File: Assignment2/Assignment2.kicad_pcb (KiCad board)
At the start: 2 copper layers, 1 part, among them U1 RP2040

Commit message: assignment2: microphone and color module
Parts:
- added C1: 10μF, Capacitor_SMD:C_0603_1608Metric, F.Cu at (106.5, 68.9)
- added C10: 100nF, Capacitor_SMD:C_0603_1608Metric, F.Cu at (106.5, 81.4)
- added C11: 100nF, Capacitor_SMD:C_0603_1608Metric, F.Cu at (106.5, 83.9)
- added C12: 100nF, Capacitor_SMD:C_0603_1608Metric, F.Cu at (110.5, 68.9)
- added C13: 100nF, Capacitor_SMD:C_0603_1608Metric, F.Cu at (110.5, 71.4)
- added C14: 100nF, Capacitor_SMD:C_0603_1608Metric, F.Cu at (110.5, 73.9)
- added C15: 100nF, Capacitor_SMD:C_0603_1608Metric, F.Cu at (110.5, 76.4)
- added C16: 100nF, Capacitor_SMD:C_0603_1608Metric, F.Cu at (110.5, 78.9)
- added C17: 10μF, Capacitor_SMD:C_0603_1608Metric, F.Cu at (110.5, 81.4)
- added C18: 0.1μF, Capacitor_SMD:C_0603_1608Metric, F.Cu at (110.5, 83.9)
- added C19: 0.1μF, Capacitor_SMD:C_0603_1608Metric, F.Cu at (114.6, 68.9)
- added C2: 10μF, Capacitor_SMD:C_0603_1608Metric, F.Cu at (106.5, 71.4)
- added C20: 200pF, Capacitor_SMD:C_0603_1608Metric, F.Cu at (114.6, 71.4)
- added C21: 100nF, Capacitor_SMD:C_0603_1608Metric, F.Cu at (114.6, 73.9)
- added C3: 100μF, Capacitor_SMD:C_0603_1608Metric, F.Cu at (106.5, 73.9)
- added C4: 15pF, Capacitor_SMD:C_0402_1005Metric, F.Cu at (120.9, 91.2)
- added C5: 15pF, Capacitor_SMD:C_0402_1005Metric, F.Cu at (120.9, 93.2)
- added C6: 1μF, Capacitor_SMD:C_0402_1005Metric, F.Cu at (120.9, 95.2)
- added C7: 100nF, Capacitor_SMD:C_0603_1608Metric, F.Cu at (106.5, 76.4)
- added C8: 100nF, Capacitor_SMD:C_0603_1608Metric, F.Cu at (106.5, 78.9)
- added C9: 1μF, Capacitor_SMD:C_0402_1005Metric, F.Cu at (120.9, 97.1)
- added H1: MountingHole, MountingHole:MountingHole_2.7mm_M2.5, F.Cu at (101.1, 71.1)
- added H2: MountingHole, MountingHole:MountingHole_2.7mm_M2.5, F.Cu at (101.1, 78.0)
- added H3: MountingHole, MountingHole:MountingHole_2.7mm_M2.5, F.Cu at (101.1, 85.0)
- added H4: MountingHole, MountingHole:MountingHole_2.7mm_M2.5, F.Cu at (101.1, 91.9)
- added J1: USB_B_Micro, Connector_USB:USB_Micro-B_Amphenol_10103594-0001LF_Horizontal, F.Cu at (125.3, 79.8)
- added J2: Conn_01x02, Connector_PinSocket_2.54mm:PinSocket_1x02_P2.54mm_Vertical, F.Cu at (106.9, 94.4)
- added J3: Conn_01x03, Connector_PinSocket_2.54mm:PinSocket_1x03_P2.54mm_Vertical, F.Cu at (117.2, 92.6)
- added J4: Conn_01x02, Connector_PinSocket_2.54mm:PinSocket_1x02_P2.54mm_Vertical, F.Cu at (111.5, 94.4)
- added MK1: SPH0645LM4H, Sensor_Audio:Knowles_SPH0645LM4H-6_3.5x2.65mm, F.Cu at (99.8, 98.1)
- added R1: 1kΩ, Resistor_SMD:R_0603_1608Metric, F.Cu at (114.6, 76.4)
- added R10: 2.2kΩ, Resistor_SMD:R_0603_1608Metric, F.Cu at (118.6, 81.4)
- added R2: DNF, Resistor_SMD:R_0603_1608Metric, F.Cu at (114.6, 78.9)
- added R3: 27Ω, Resistor_SMD:R_0603_1608Metric, F.Cu at (114.6, 81.4)
- added R4: 27Ω, Resistor_SMD:R_0603_1608Metric, F.Cu at (114.6, 83.9)
- added R5: 1MΩ, Resistor_SMD:R_0603_1608Metric, F.Cu at (118.6, 68.9)
- added R6: 51Ω, Resistor_SMD:R_0603_1608Metric, F.Cu at (118.6, 71.4)
- added R7: 51Ω, Resistor_SMD:R_0603_1608Metric, F.Cu at (118.6, 73.9)
- added R8: 51Ω, Resistor_SMD:R_0603_1608Metric, F.Cu at (118.6, 76.4)
- added R9: 2.2kΩ, Resistor_SMD:R_0603_1608Metric, F.Cu at (118.6, 78.9)
- added SW1: SW_Push, Button_Switch_THT:SW_PUSH_1P1T_6x3.5mm_H4.3_APEM_MJTP1243, F.Cu at (116.8, 87.7)
- added U2: NCP1117-3.3_SOT223, Package_TO_SOT_SMD:SOT-223-3_TabPin2, F.Cu at (125.5, 71.8)
- added U3: W25Q128JVS, Package_SO:SOIC-8_5.3x5.3mm_P1.27mm, F.Cu at (109.7, 88.6)
- added U4: ABM8-272-T3, ABM8-272-T3:ABM8-272-T3, F.Cu at (125.4, 97.7)
- added U5: MAX98357A, Package_DFN_QFN:TQFN-16-1EP_3x3mm_P0.5mm_EP1.23x1.23mm, F.Cu at (125.0, 92.9)
- added U6: VEML6040, VEML6040:VISHAY_VEML6040_1.25X2X1, F.Cu at (128.0, 86.6)
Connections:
- U1 pad 1: Net-(U1-IOVDD-Pad1) -> +3.3V
- U1 pad 10: Net-(U1-IOVDD-Pad1) -> +3.3V
- U1 pad 19: unconnected-(U1-TESTEN-Pad19) -> GND
- U1 pad 2: unconnected-(U1-GPIO0-Pad2) -> /GPIO0
- U1 pad 20: unconnected-(U1-XIN-Pad20) -> /XIN
- U1 pad 21: unconnected-(U1-XOUT-Pad21) -> /XOUT
- U1 pad 22: Net-(U1-IOVDD-Pad1) -> +3.3V
- U1 pad 23: Net-(U1-DVDD-Pad23) -> +1V1
- U1 pad 24: unconnected-(U1-SWCLK-Pad24) -> /SWCLK
- U1 pad 25: unconnected-(U1-SWD-Pad25) -> /SWD
- U1 pad 26: unconnected-(U1-RUN-Pad26) -> /RUN
- U1 pad 3: unconnected-(U1-GPIO1-Pad3) -> /GPIO1
- U1 pad 33: Net-(U1-IOVDD-Pad1) -> +3.3V
- U1 pad 4: unconnected-(U1-GPIO2-Pad4) -> /GPIO2
- U1 pad 42: Net-(U1-IOVDD-Pad1) -> +3.3V
- U1 pad 43: unconnected-(U1-ADC_AVDD-Pad43) -> +3.3V
- U1 pad 44: unconnected-(U1-VREG_IN-Pad44) -> +3.3V
- U1 pad 45: unconnected-(U1-VREG_VOUT-Pad45) -> +1V1
- U1 pad 46: unconnected-(U1-USB_DM-Pad46) -> Net-(U1-USB_DM)
- U1 pad 47: unconnected-(U1-USB_DP-Pad47) -> Net-(U1-USB_DP)
- U1 pad 48: unconnected-(U1-USB_VDD-Pad48) -> +3.3V
- U1 pad 49: Net-(U1-IOVDD-Pad1) -> +3.3V
- U1 pad 5: unconnected-(U1-GPIO3-Pad5) -> /GPIO3
- U1 pad 50: Net-(U1-DVDD-Pad23) -> +1V1
- U1 pad 51: unconnected-(U1-QSPI_SD3-Pad51) -> /QSPI_SD3
- U1 pad 52: unconnected-(U1-QSPI_SCLK-Pad52) -> /QSPI_SCLK
- U1 pad 53: unconnected-(U1-QSPI_SD0-Pad53) -> /QSPI_SD0
- U1 pad 54: unconnected-(U1-QSPI_SD2-Pad54) -> /QSPI_SD2
- U1 pad 55: unconnected-(U1-QSPI_SD1-Pad55) -> /QSPI_SD1
- U1 pad 56: unconnected-(U1-QSPI_SS-Pad56) -> /QSPI_SS
- U1 pad 57: unconnected-(U1-GND-Pad57) -> GND
- U1 pad 6: unconnected-(U1-GPIO4-Pad6) -> /GPIO4
- U1 pad 7: unconnected-(U1-GPIO5-Pad7) -> /GPIO5
- U1 pad 8: unconnected-(U1-GPIO6-Pad8) -> /GPIO6
- U1 pad 9: unconnected-(U1-GPIO7-Pad9) -> /GPIO7

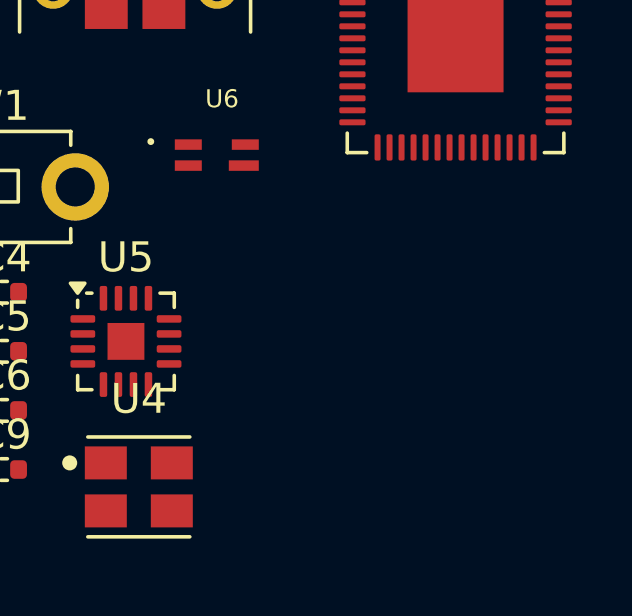
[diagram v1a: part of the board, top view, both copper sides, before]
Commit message: assignment2: add leds
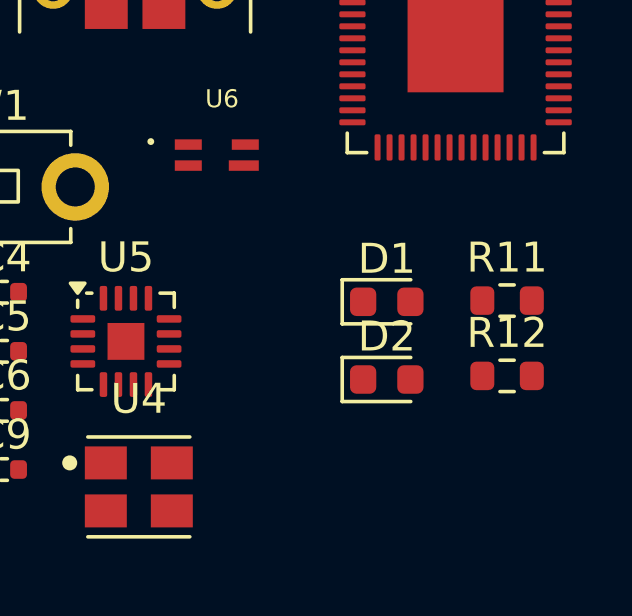
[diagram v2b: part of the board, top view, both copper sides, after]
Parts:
- added D1: LED, LED_SMD:LED_0603_1608Metric, F.Cu at (133.7, 91.5)
- added D2: LED, LED_SMD:LED_0603_1608Metric, F.Cu at (133.7, 94.1)
- added R11: 150Ω, Resistor_SMD:R_0603_1608Metric, F.Cu at (137.7, 91.5)
- added R12: 150Ω, Resistor_SMD:R_0603_1608Metric, F.Cu at (137.7, 94.0)
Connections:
- U1 pad 11: unconnected-(U1-GPIO8-Pad11) -> /GPIO8
- U1 pad 12: unconnected-(U1-GPIO9-Pad12) -> /GPIO9

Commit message: route
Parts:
- moved H2 49.6 mm to (145.0, 55.0)
- moved H4 44.1 mm to (145.0, 95.0)
- moved J2 42.5 mm to (110.2, 52.0), turned to 90 degrees
- moved C2 34.5 mm to (140.8, 67.2)
- moved C16 31.5 mm to (141.4, 72.7), turned to 90 degrees
- moved SW1 30.1 mm to (146.4, 82.5), turned to -90 degrees
- moved C9 29.2 mm to (124.5, 68.1), turned to 90 degrees
- moved C15 29.2 mm to (139.5, 72.7), turned to 90 degrees
- moved C1 29.2 mm to (133.8, 58.5)
- moved C11 27.6 mm to (131.8, 72.7), turned to 90 degrees
- moved U3 27.3 mm to (116.8, 62.3)
- moved C6 27.2 mm to (123.5, 68.1), turned to 90 degrees
- moved C14 27.0 mm to (137.5, 72.7), turned to 90 degrees
- moved J1 26.7 mm to (126.5, 53.1), turned to 180 degrees
- moved Ue 26.5 mm to (101.8, 90.0), turned to 90 degrees
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- renumbered U6 to Ue
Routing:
- net GND: track 0.00 -> 92.3 mm, vias 0 -> 16
- net +3.3V: track 0.00 -> 46.0 mm, vias 0 -> 6
- net /GPIO7: track 0.00 -> 27.3 mm
- net /QSPI_SS: track 0.00 -> 27.1 mm
- net /GPIO6: track 0.00 -> 26.2 mm, vias 0 -> 2
- net /SWD: track 0.00 -> 25.1 mm
- net /RUN: track 0.00 -> 24.3 mm
- net /USB_D+: track 0.00 -> 23.2 mm
- net /SWCLK: track 0.00 -> 23.1 mm
- net /QSPI_SD1: track 0.00 -> 21.3 mm
- net Net-(MK1-BCLK): track 0.00 -> 21.3 mm
- net /QSPI_SD2: track 0.00 -> 19.9 mm
- net +1V1: track 0.00 -> 19.1 mm, vias 0 -> 3
- net /GPIO8: track 0.00 -> 15.3 mm
- net /GPIO9: track 0.00 -> 13.7 mm
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- added copper zone on F.Cu, net +3.3V
- added copper zone on F.Cu, net +5V
- added copper zone on B.Cu, net GND
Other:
- board outline added: 50 x 50 mm

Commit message: swap c19 and c20, add silkscreen and round corner
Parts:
- moved C20 1.80 mm to (105.2, 81.6)
- moved C19 1.80 mm to (107.0, 81.6)
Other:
- outline, holes or cut-outs redrawn
- board text added: "SWD Debug"
- board text added: "Speaker"
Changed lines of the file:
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@@
 	(footprint "Capacitor_SMD:C_0603_1608Metric"
 		(layer "F.Cu")
-		(at 107 81.575 90)
+		(at 105.2 81.6 90)
 		(descr "Capacitor SMD 0603 (1608 Metric), square (rectangular) end terminal, IPC_7351 nominal, (Body size source: IPC-SM-782 page 76, https://www.pcb-3d.com/wordpress/wp-content/uploads/ipc-sm-782a_amendment_1_and_2.pdf), generated with kicad-footprint-generator")
 		(tags "capacitor")
 		(property "Reference" "C20"
-			(at 0.075 1.5 90)
+			(at 2.1 0 180)
 			(layer "F.SilkS")
 			(effects
@@
 			(at 0 -3.7 0)
 			(layer "F.SilkS")
+			(hide yes)
 			(effects
 				(font
@@
 			(at 0 -3.7 0)
 			(layer "F.SilkS")
+			(hide yes)
 			(effects
 				(font
@@
 			(at 0.1 3.8 0)
 			(layer "F.SilkS")
+			(hide yes)
 			(effects
 				(font
@@
 	(footprint "Capacitor_SMD:C_0603_1608Metric"
 		(layer "F.Cu")
-		(at 105.2 81.6 90)
+		(at 107 81.6 90)
 		(descr "Capacitor SMD 0603 (1608 Metric), square (rectangular) end terminal, IPC_7351 nominal, (Body size source: IPC-SM-782 page 76, https://www.pcb-3d.com/wordpress/wp-content/uploads/ipc-sm-782a_amendment_1_and_2.pdf), generated with kicad-footprint-generator")
 		(tags "capacitor")
 		(property "Reference" "C19"
-			(at 2.2 0.5 180)
+			(at 0.1 1.5 270)
 			(layer "F.SilkS")
 			(effects
@@
 			(at 0 -3.7 0)
 			(layer "F.SilkS")
+			(hide yes)
 			(effects
 				(font
@@
 		)
 	)
-	(gr_rect
-		(start 100 50)
-		(end 150 100)
+	(gr_line
+		(start 105 100)
+		(end 145 100)
+		(stroke
+			(width 0.5)
+			(type solid)
+		)
+		(layer "Edge.Cuts")
+	)
+	(gr_arc
+		(start 105 100)
+		(mid 101.464466 98.535534)
+		(end 100 95)
+		(stroke
+			(width 0.5)
+			(type solid)
+		)
+		(layer "Edge.Cuts")
+	)
+	(gr_arc
+		(start 100 55)
+		(mid 101.464466 51.464466)
+		(end 105 50)
+		(stroke
+			(width 0.5)
+			(type solid)
+		)
+		(layer "Edge.Cuts")
+	)
+	(gr_arc
+		(start 145 50)
+		(mid 148.535534 51.464466)
+		(end 150 55)
+		(stroke
+			(width 0.5)
+			(type solid)
+		)
+		(layer "Edge.Cuts")
+	)
+	(gr_line
+		(start 150 95)
+		(end 150 55)
+		(stroke
+			(width 0.5)
+			(type solid)
+		)
+		(layer "Edge.Cuts")
+	)
+	(gr_line
+		(start 105 50)
+		(end 145 50)
+		(stroke
+			(width 0.5)
+			(type solid)
+		)
+		(layer "Edge.Cuts")
+	)
+	(gr_line
+		(start 100 55)
+		(end 100 95)
+		(stroke
+			(width 0.5)
+			(type solid)
+		)
+		(layer "Edge.Cuts")
+	)
+	(gr_arc
+		(start 150 95)
+		(mid 148.535534 98.535534)
+		(end 145 100)
 		(stroke
 			(width 0.5)
 			(type solid)
 		)
-		(fill no)
 		(layer "Edge.Cuts")
 	)
+	(gr_text "SWD Debug"
+		(at 135.5 95 0)
+		(layer "F.SilkS")
+		(effects
+			(font
+				(size 1 1)
+				(thickness 0.1)
+			)
+			(justify bottom)
+		)
+	)
+	(gr_text "Speaker"
+		(at 105.5 72 90)
+		(layer "F.SilkS")
+		(effects
+			(font
+				(size 1 1)
+				(thickness 0.1)
+			)
+			(justify bottom)
+		)
+	)
 	(segment
 		(start 127.84 56.002)
@@
 	)
 	(segment
+		(start 106 83.8)
+		(end 106 83.175)
+		(width 0.2)
+		(layer "F.Cu")
+		(net 4)
+	)
+	(segment
 		(start 125.31 52.02)
 		(end 125.58 51.75)
@@
 	)
 	(segment
-		(start 105.2 82.375)
-		(end 106 83.175)
-		(width 0.2)
-		(layer "F.Cu")
-		(net 4)
-	)
-	(segment
 		(start 101.2 85.4)
 		(end 101.225 85.425)
@@
 	)
 	(segment
+		(start 106 83.175)
+		(end 105.2 82.375)
+		(width 0.2)
+		(layer "F.Cu")
+		(net 4)
+	)
+	(segment
 		(start 125.5 82.7)
 		(end 125.5 83.6)
@@
 	)
 	(segment
-		(start 107 82.35)
-		(end 106.175 83.175)
-		(width 0.2)
-		(layer "F.Cu")
-		(net 4)
-	)
-	(segment
 		(start 103.279808 83.4)
 		(end 103.4 83.279808)
@@
 	)
 	(segment
-		(start 106 83.175)
-		(end 106 83.8)
-		(width 0.2)
-		(layer "F.Cu")
-		(net 4)
-	)
-	(segment
 		(start 119.5 83.4)
 		(end 119.5 84.8)
@@
 	)
 	(segment
-		(start 106.175 83.175)
-		(end 106 83.175)
+		(start 124.55 66.5872)
+		(end 124.079 66.1162)
 		(width 0.2)
 		(layer "F.Cu")
@@
 	)
 	(segment
-		(start 124.55 66.5872)
-		(end 124.079 66.1162)
+		(start 106.8 82.375)
+		(end 107 82.375)
 		(width 0.2)
 		(layer "F.Cu")
@@
 		(net 4)
 	)
+	(segment
+		(start 106 83.175)
+		(end 106.8 82.375)
+		(width 0.2)
+		(layer "F.Cu")
+		(net 4)
+	)
 	(via
 		(at 101.3 92.6)
@@
 			(pts
 				(xy 127 71.745682) (xy 127 70.295682) (xy 131 70.295682) (xy 131 63.045682) (xy 134 63.045682) (xy 134 58.545682)
-				(xy 137.5 58.545682) (xy 137.5 55.545682) (xy 137.5 55.545682) (xy 137.5 50.045682) (xy 149.5 50.045682)
-				(xy 149.5552 98.885082) (xy 100.5 99.045682) (xy 100.5 93.245682) (xy 100.5 87.245682) (xy 101.9 87.245682)
-				(xy 101.9 85.145682) (xy 105.6 85.145682) (xy 105.6 82.445682) (xy 103.1 82.545682) (xy 103.1 79.045682)
-				(xy 117 79) (xy 120.5 79) (xy 118.5 86.5) (xy 129.1 86.30672) (xy 129.1 77.860087) (xy 121.05 77.804873)
-				(xy 121.05 71.745682)
+				(xy 137.5 58.545682) (xy 137.5 55.545682) (xy 137.5 50.045682) (xy 149.5 50.045682) (xy 149.5552 98.885082)
+				(xy 100.5 99.045682) (xy 100.5 93.245682) (xy 100.5 87.245682) (xy 101.9 87.245682) (xy 101.9 85.145682)
+				(xy 105.6 85.145682) (xy 105.6 82.445682) (xy 103.1 82.545682) (xy 103.1 79.045682) (xy 117 79)
+				(xy 120.5 79) (xy 118.5 86.5) (xy 129.1 86.30672) (xy 129.1 77.860087) (xy 121.05 77.804873) (xy 121.05 71.745682)
 			)
 		)
